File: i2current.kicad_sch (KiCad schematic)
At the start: 44 parts, among them J1 Jack-DC, J2 USB_C_Receptacle_USB2.0, J3 CONN_BATT, SW1 SW_SPDT, U1 TPS61022, U2 BQ25606RGER, U3 SPX3819M5-L-3-3, U4 FUSB302B01MPX

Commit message: save before charger replace
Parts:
- removed D2: D_Schottky, Diode_SMD:D_SMA, symbol Device:D_Schottky
- removed J1: Jack-DC, Connector_BarrelJack:BarrelJack_CUI_PJ-102AH_Horizontal, symbol Connector:Jack-DC
- added J1: Barrel_Jack_Switch, Connector_BarrelJack:BarrelJack_Wuerth_6941xx301002, symbol Connector:Barrel_Jack_Switch
- added Q1: WST03P06, Package_TO_SOT_SMD:SOT-23, symbol Critbit_lib:WST03P06
- added R4: 10k, Resistor_SMD:R_0402_1005Metric, symbol Device:R_Small
- added U4: ~, Critbit_lib:OLED_4Pin_128x64_new, symbol Critbit_lib:OLED_4Pin
- added U6: XT30(2+2)PW-M.G.B, crap:CONN-TH_4P-XT30PW-M, symbol easyeda2kicad:XT30(2+2)PW-M.G.B
- added U8: BQ25792RQMR, easyeda2kicad:QFN-29_L4.0-W4.0-P0.40-TL-BQ25792RQMR, symbol easyeda2kicad:BQ25792RQMR
- D1: value D_Schottky -> 1N5819WS; footprint Diode_SMD:D_SMA -> Diode_SMD:D_SOD-323; LCSC (none) -> C191023
- J3: footprint (none) -> Connector_JST:JST_XH_S3B-XH-A_1x03_P2.50mm_Horizontal
- L1, L2: footprint (none) -> Inductor_SMD:L_AVX_LMLP07A7
- renumbered D3 to D2, R9 to R10, R10 to R11, R11 to R12, R12 to R13, R13 to R14, R4 to R5, R5 to R6, R6 to R7, R7 to R8, R8 to R9, U4 to U5
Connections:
- net +BATT: now also U6.1
- net BAT: now also U8.22 (BAT), U8.23 (BAT)
- net GND: now also J1.2
- net VBUS: now also JP3.2 (B), Q1.3 (S), R4.2, U8.2 (VBUS), U8.3 (VBUS); no longer JP3.1 (A)
- net BQ_PWR: now reaches C1.1, D1.1 (K), U2.1 (VAC), U2.24 (VBUS)
- net BQ_PWR: now also JP1.1 (A), JP3.1 (A), Q1.2 (D); no longer JP1.2 (B), JP3.2 (B)
- net at D1.2 (A): now also JP1.2 (B), J1.1; no longer JP1.1 (A)
- new net PUSB_OFF: J1.3, Q1.1 (G), R4.1
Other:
- moved on the sheet: C1, C10, C2, C3, C4, C5, C6, C7, C8, C9, D2, J3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

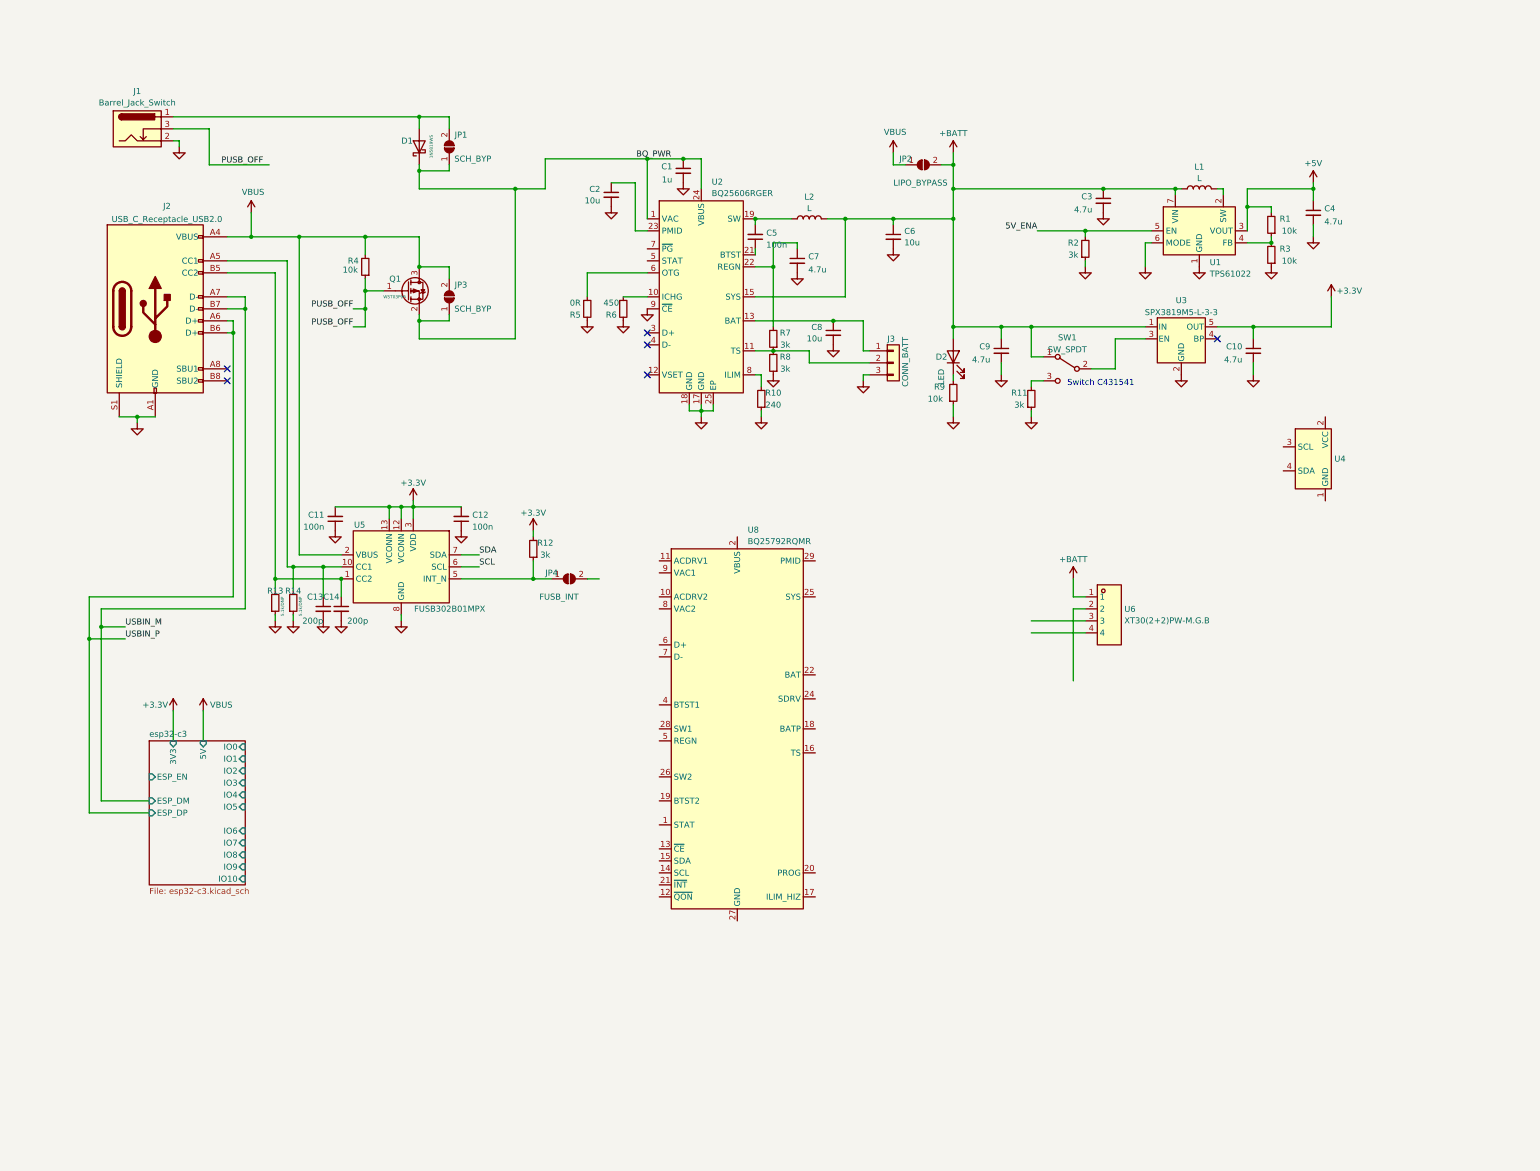
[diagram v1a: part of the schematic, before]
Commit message: connector placement
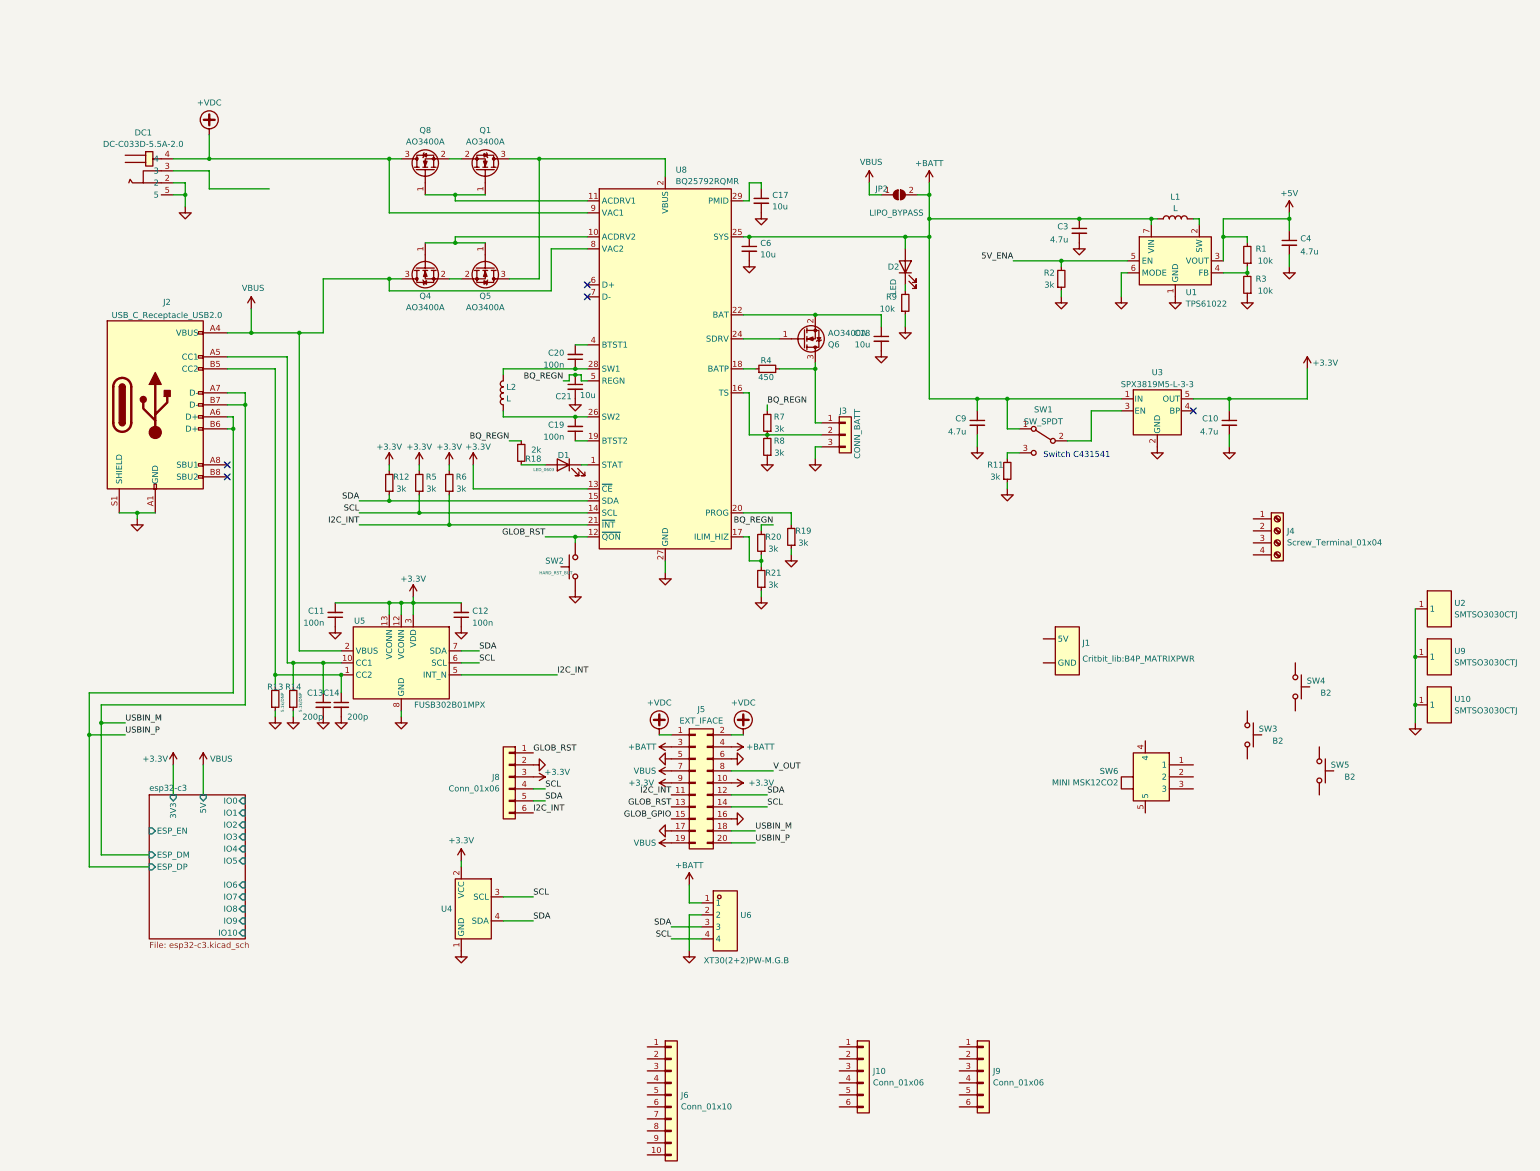
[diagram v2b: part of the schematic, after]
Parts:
- removed C1: 1u, Capacitor_SMD:C_0402_1005Metric, symbol Device:C_Small
- removed C2, C8: 10u, Capacitor_SMD:C_0402_1005Metric, symbol Device:C_Small
- removed C5: 100n, Capacitor_SMD:C_0402_1005Metric, symbol Device:C_Small
- removed C7: 4.7u, Capacitor_SMD:C_0402_1005Metric, symbol Device:C_Small
- removed D1: 1N5819WS, Diode_SMD:D_SOD-323, symbol Device:D_Schottky
- removed J1: Barrel_Jack_Switch, Connector_BarrelJack:BarrelJack_Wuerth_6941xx301002, symbol Connector:Barrel_Jack_Switch
- removed JP1, JP3: SCH_BYP, Jumper:SolderJumper-2_P1.3mm_Open_TrianglePad1.0x1.5mm, symbol Jumper:SolderJumper_2_Open
- removed JP4: FUSB_INT, Jumper:SolderJumper-2_P1.3mm_Open_TrianglePad1.0x1.5mm, symbol Jumper:SolderJumper_2_Open
- removed Q1: WST03P06, Package_TO_SOT_SMD:SOT-23, symbol Critbit_lib:WST03P06
- removed R10: 240, Resistor_SMD:R_0402_1005Metric, symbol Device:R_Small
- removed U2: BQ25606RGER, easyeda2kicad:VQFN-24_L4.0-W4.0-P0.50-TL-EP2.8, symbol easyeda2kicad:BQ25606RGER
- added C17, C18, C21: 10u, Capacitor_SMD:C_0402_1005Metric, symbol Device:C_Small
- added C19, C20: 100n, Capacitor_SMD:C_0402_1005Metric, symbol Device:C_Small
- added D1: LED_0603, LED_SMD:LED_0603_1608Metric_Pad1.05x0.95mm_HandSolder, symbol Device:LED
- added DC1: DC-C033D-5.5A-2.0, easyeda2kicad:DC-IN-TH_DC-C033D-5.5A-2.5, symbol easyeda2kicad:DC-C033D-5.5A-2.0
- added J1: ~, Critbit_lib:B4P_MATRIXPWR, symbol Critbit_lib:MATRIXPWR
- added J10, J9: Conn_01x06, Connector_JST:JST_PH_S6B-PH-K_1x06_P2.00mm_Horizontal, symbol Connector_Generic:Conn_01x06
- added J4: Screw_Terminal_01x04, TerminalBlock:TerminalBlock_bornier-4_P5.08mm, symbol Connector:Screw_Terminal_01x04
- added J5: EXT_IFACE, Critbit_lib:2x10_smdthrough, symbol Connector_Generic:Conn_02x10_Odd_Even
- added J6: Conn_01x10, Connector_Molex:Molex_PicoBlade_53261-1071_1x10-1MP_P1.25mm_Horizontal, symbol Connector_Generic:Conn_01x10
- added J8: Conn_01x06, Connector_PinHeader_2.54mm:PinHeader_1x06_P2.54mm_Vertical, symbol Connector_Generic:Conn_01x06
- added Q1, Q4, Q5, Q6, Q8: AO3400A, Package_TO_SOT_SMD:SOT-23, symbol Transistor_FET:AO3400A
- added R18: 2k, Resistor_SMD:R_0402_1005Metric, symbol Device:R_Small
- added R19, R20, R21: 3k, Resistor_SMD:R_0402_1005Metric, symbol Device:R_Small
- added SW2: HARD_RST_BUT, Button_Switch_SMD:SW_SPST_TL3342, symbol Switch:SW_Push
- added SW3, SW4, SW5: B2, Button_Switch_SMD:SW_SPST_EVQP7C, symbol Switch:SW_Push
- added SW6: MINI MSK12CO2, easyeda2kicad:SW-SMD_MSK12CO2, symbol easyeda2kicad:MINIMSK12CO2
- added U10, U2, U9: SMTSO3030CTJ, easyeda2kicad:SMD_BD5.6-D4.1, symbol easyeda2kicad:SMTSO3030CTJ
- J3: footprint Connector_JST:JST_XH_S3B-XH-A_1x03_P2.50mm_Horizontal -> Connector_JST:JST_PH_S3B-PH-K_1x03_P2.00mm_Horizontal
- R4: value 10k -> 450; LCSC C25744 -> C25890
- R5: value 0R -> 3k
- R6: value 450 -> 3k
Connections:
- net PUSB_OFF is gone; now on an unnamed net: R4.1
- net +3.3V: now also R5.2, R6.2, U4.2 (VCC), U8.13 (~{CE}), J5.10 (Pin_10), J5.9 (Pin_9), J8.3 (Pin_3)
- net +BATT: now also U8.25 (SYS), J5.3 (Pin_3), J5.4 (Pin_4); no longer L2.2
- net BAT: now also C18.1, Q6.2 (S); no longer J3.1 (Pin_1)
- net GND: now also U4.1 (GND), U6.2, U8.27 (GND), C17.2, C18.2, C21.2, DC1.2, DC1.5, J5.16 (Pin_16), J5.17 (Pin_17), J5.5 (Pin_5), J5.6 (Pin_6), J8.2 (Pin_2), R19.1, R21.1, SW2.1, U10.1, U2.1, U9.1; no longer R5.2, R6.2
- net SCL: now also R5.1, U4.3 (SCL), U6.4, U8.14 (SCL), J5.14 (Pin_14), J8.4 (Pin_4)
- net SDA: now also R12.1, U4.4 (SDA), U6.3, U8.15 (SDA), J5.12 (Pin_12), J8.5 (Pin_5)
- net USBIN_M: now also J5.18 (Pin_18)
- net USBIN_P: now also J5.20 (Pin_20)
- net VBUS: now also U8.8 (VAC2), J5.19 (Pin_19), J5.7 (Pin_7), Q1.3 (D), Q4.3 (D), Q5.3 (D); no longer R4.2
- net at L2.1: now also U8.26 (SW2), C19.2
- net I2C_INT: now reaches R6.1
- net I2C_INT: now also U5.5 (INT_N), U8.21 (~{INT}), J5.11 (Pin_11), J8.6 (Pin_6)
- net at J3.2 (Pin_2), R7.1, R8.2: now also U8.16 (TS)
- net BQ_REGN: now reaches R7.2
- net BQ_REGN: now also U8.5 (REGN), C21.1, R18.1, R20.2
- net at U8.1 (STAT): now also D1.1 (K)
- net at U8.10 (ACDRV2): now also Q4.1 (G), Q5.1 (G)
- net at U8.11 (ACDRV1): now also Q1.1 (G), Q8.1 (G)
- net GLOB_RST: now reaches U8.12 (~{QON})
- net GLOB_RST: now also J5.13 (Pin_13), J8.1 (Pin_1), SW2.2
- net at U8.17 (ILIM_HIZ): now also R20.1, R21.2
- net at U8.19 (BTST2): now also C19.1
- net at U8.20 (PROG): now also R19.2
- net at U8.24 (SDRV): now also Q6.1 (G)
- net at U8.28 (SW1): now also L2.2, C20.1
- net at U8.29 (PMID): now also C17.1
- net at U8.4 (BTST1): now also C20.2
- net +VDC: now reaches U8.9 (VAC1)
- net +VDC: now also DC1.4, J5.1 (Pin_1), J5.2 (Pin_2), Q8.3 (D)
- new net: Q4.2 (S), Q5.2 (S)
- new net: J3.1 (Pin_1), Q6.3 (D), R4.2
- new net: Q1.2 (S), Q8.2 (S)
- new net: D1.2 (A), R18.2
- new net GLOB_GPIO: J5.15 (Pin_15)
- new net V_OUT: J5.8 (Pin_8)
- no-connect marks 6 -> 5
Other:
- moved on the sheet: C10, C11, C12, C13, C14, C3, C4, C6, C9, D2, J2, J3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

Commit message: adadadadadadadadadada
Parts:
- removed J10: Conn_01x06, Connector_JST:JST_PH_S6B-PH-K_1x06_P2.00mm_Horizontal, symbol Connector_Generic:Conn_01x06
- removed J4: Screw_Terminal_01x04, TerminalBlock:TerminalBlock_bornier-4_P5.08mm, symbol Connector:Screw_Terminal_01x04
- removed L2: L, Inductor_SMD:L_AVX_LMLP07A7, symbol Device:L
- removed R11: 3k, Resistor_SMD:R_0402_1005Metric, symbol Device:R_Small
- removed R14: 5.1k/DNP, Resistor_SMD:R_0201_0603Metric, symbol Device:R_Small
- removed SW1: SW_SPDT, Button_Switch_SMD:SW_SPDT_PCM12, symbol Switch:SW_SPDT
- removed SW5: B2, Button_Switch_SMD:SW_SPST_EVQP7C, symbol Switch:SW_Push
- removed SW6: MINI MSK12CO2, easyeda2kicad:SW-SMD_MSK12CO2, symbol easyeda2kicad:MINIMSK12CO2
- removed U4: ~, Critbit_lib:OLED_4Pin_128x64_new, symbol Critbit_lib:OLED_4Pin
- added C1, C2: 100n, Capacitor_SMD:C_0402_1005Metric, symbol Device:C_Small
- added J11, J12: Screw_Terminal_01x02, TerminalBlock_MetzConnect:TerminalBlock_MetzConnect_Type086_RT03402HBLC_1x02_P3.81mm_Horizontal, symbol Connector:Screw_Terminal_01x02
- added L3: FXL0420-1R0-M, easyeda2kicad:IND-SMD_L4.4-W4.2, symbol easyeda2kicad:FXL0420-1R0-M
- added R10: 5.1k/DNP, Resistor_SMD:R_0603_1608Metric_Pad0.98x0.95mm_HandSolder, symbol Device:R_Small
- added SW6: SW_SPDT, Button_Switch_THT:SW_Slide_SPDT_Angled_CK_OS102011MA1Q, symbol Switch:SW_SPDT
- C10, C17, C18, C21, C3, C4, C6, C9: LCSC C19702 -> (none)
- C11, C12, C19, C20: LCSC C307331 -> (none)
- C13, C14: LCSC C1530 -> (none)
- JP2: LCSC DNP -> (none)
- R1, R3, R9: LCSC C25768 -> (none)
- R12, R19, R20, R21, R4, R5, R6, R7, R8: LCSC C25890 -> (none)
- R13: footprint Resistor_SMD:R_0201_0603Metric -> Resistor_SMD:R_0603_1608Metric_Pad0.98x0.95mm_HandSolder; LCSC C25117 -> (none)
- SW3, SW4: footprint Button_Switch_SMD:SW_SPST_EVQP7C -> Button_Switch_SMD:SW_SPST_TL3342
- U5: LCSC C132291 -> (none)
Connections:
- net V_OUT is gone; now on net I2C_INT: J5.8 (Pin_8)
- net +3.3V: now also J6.5 (Pin_5)
- net +BATT: now also J6.2 (Pin_2), U3.3 (EN)
- net +VDC: now also J6.1 (Pin_1)
- net GLOB_RST: now also J5.11 (Pin_11); no longer J5.13 (Pin_13)
- net GND: now also J6.3 (Pin_3), J6.8 (Pin_8), J9.1 (Pin_1), SW3.1, SW4.1, C1.2, C2.2, R10.1
- net I2C_INT: now also J6.4 (Pin_4); no longer J5.11 (Pin_11)
- net SCL: now also J6.7 (Pin_7)
- net SDA: now also J6.6 (Pin_6)
- net USBIN_M: now also J6.9 (Pin_9), J9.3 (Pin_3)
- net USBIN_P: now also J6.10 (Pin_10), J9.4 (Pin_4)
- net VBUS: now also J9.6 (Pin_6); no longer Q1.3 (D), Q5.3 (D), U8.2 (VBUS), U8.3 (VBUS)
- net esp32-c3/ESP_EN: now also SW3.2, C1.1
- net esp32-c3/IO9: now also SW4.2, C2.1
- net CC2: now reaches J2.B5 (CC2), R13.2, U5.1 (CC2), U5.14 (CC2)
- net CC2: now also C13.1, J9.5 (Pin_5); no longer C14.1
- net at C19.2, U8.26 (SW2): now also L3.2
- net at C20.1, U8.28 (SW1): now also L3.1
- net CC1: now reaches J9.2 (Pin_2)
- net CC1: now also C14.1, J2.A5 (CC1), U5.10 (CC1), U5.11 (CC1), R10.2
- net GLOB_GPIO renamed GLOB_GPIO2
- new net GLOB_GPIO1: J5.13 (Pin_13)
- new net VBUS_PIN: Q1.3 (D), Q5.3 (D), U8.2 (VBUS_PIN), U8.3 (VBUS_PIN)
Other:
- note added: "C157919"
- note added: "C393937"
- note added: "C500113"
- note removed: "Switch C431541"
- moved on the sheet: C10, C11, C12, C13, C14, C20, C21, C9, J1, J5, J6, J8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

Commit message: do backup kids
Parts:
- removed J11, J12: Screw_Terminal_01x02, TerminalBlock_MetzConnect:TerminalBlock_MetzConnect_Type086_RT03402HBLC_1x02_P3.81mm_Horizontal, symbol Connector:Screw_Terminal_01x02
- removed L1: L, Inductor_SMD:L_AVX_LMLP07A7, symbol Device:L
- removed SW2: HARD_RST_BUT, Button_Switch_SMD:SW_SPST_TL3342, symbol Switch:SW_Push
- removed U1: TPS61022, Package_DFN_QFN:Texas_RWU0007A_VQFN-7_2x2mm_P0.5mm, symbol Converter_DCDC:TPS61022
- removed U3: SPX3819M5-L-3-3, Package_TO_SOT_SMD:SOT-23-5, symbol Regulator_Linear:SPX3819M5-L-3-3
- removed U6: XT30(2+2)PW-M.G.B, crap:CONN-TH_4P-XT30PW-M, symbol easyeda2kicad:XT30(2+2)PW-M.G.B
- added C22, C25, C27, C35, C36, C38, C7, C8: 100n, Capacitor_SMD:C_0402_1005Metric, symbol Device:C_Small
- added C23, C24, C28: 22uF, Capacitor_SMD:C_0603_1608Metric, symbol Device:C_Small
- added C26, C31, C32, C33, C34, C37, C39, C40, C41, C42, C5: 10u, Capacitor_SMD:C_0603_1608Metric, symbol Device:C_Small
- added C29, C30: 2u2, Capacitor_SMD:C_0603_1608Metric, symbol Device:C_Small
- added D3: 1N5819WS, Diode_SMD:D_SOD-323, symbol Device:D_Schottky
- added J10, J11: QWIIC, Connector_JST:JST_SH_SM04B-SRSS-TB_1x04-1MP_P1.00mm_Horizontal, symbol Connector_Generic:Conn_01x04
- added J4: BIG_OUT, TerminalBlock_MetzConnect:TerminalBlock_MetzConnect_Type086_RT03406HBLC_1x06_P3.81mm_Horizontal, symbol Connector:Screw_Terminal_01x06
- added JP1: HARDRST, Jumper:SolderJumper-2_P1.3mm_Open_TrianglePad1.0x1.5mm, symbol Jumper:SolderJumper_2_Open
- added L1: IHLP3232DZER3R3M11, easyeda2kicad:IND-SMD_L8.7-W8.2_IHLP-3232CZ, symbol easyeda2kicad:IHLP3232DZER3R3M11
- added L4: FXL0630-6R8-M, easyeda2kicad:IND-SMD_L7.0-W6.6, symbol easyeda2kicad:FXL0630-6R8-M
- added R11, R14, R16, R17: 3k, Resistor_SMD:R_0402_1005Metric, symbol Device:R_Small
- added R22: 450, Resistor_SMD:R_0402_1005Metric, symbol Device:R_Small
- added R23, R24: 2, Resistor_SMD:R_0402_1005Metric, symbol Device:R_Small
- added U11: TPS56637RPAR, easyeda2kicad:VQFN-HR-10_L3.0-W3.0_RPA, symbol easyeda2kicad:TPS56637RPAR
- added U3: SMTSO3030CTJ, easyeda2kicad:SMD_BD5.6-D4.1, symbol easyeda2kicad:SMTSO3030CTJ
- added U4: TPS5430DDA, Package_SO:SOIC-8_3.9x4.9mm_P1.27mm, symbol Critbit_lib:TPS54331
- C10, C9: value 4.7u -> 100n
- C17, C18, C6: footprint Capacitor_SMD:C_0402_1005Metric -> Capacitor_SMD:C_0603_1608Metric
- C21: value 10u -> 4.7u/10V
- C3: value 4.7u -> 22uF; footprint Capacitor_SMD:C_0402_1005Metric -> Capacitor_SMD:C_0603_1608Metric
- C4: value 4.7u -> 10u; footprint Capacitor_SMD:C_0402_1005Metric -> Capacitor_SMD:C_0603_1608Metric
- R1: value 10k -> 73.2k
- R19: footprint Resistor_SMD:R_0402_1005Metric -> Resistor_SMD:R_0603_1608Metric_Pad0.98x0.95mm_HandSolder
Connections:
- net +3.3V: now also C3.1, C23.1, C24.1, C28.1, J10.2 (Pin_2), J11.2 (Pin_2), L4.1, R11.2; no longer C10.1, U8.13 (~{CE})
- net +5V: now also J1.5V, C41.1, C42.1, L1.2
- net +BATT: now also C26.1, C27.2, C31.1, C32.1, C36.2, C37.1, C5.1, C7.2, J4.1 (Pin_1), R22.2, U11.8 (VIN), U4.2 (VIN); no longer C3.1, C9.1, D2.2 (A)
- net +VDC: now also J4.3 (Pin_3), R23.2
- net 5V_ENA: now also R2.1, U11.1 (EN); no longer R2.2
- net BQ_REGN: now also U8.13 (~{CE})
- net GLOB_RST: no longer J5.11 (Pin_11), U8.12 (~{QON})
- net GND: now also C10.1, C9.1, J1.GND, SW6.3 (C), C23.2, C24.2, C26.2, C27.1, C28.2, C29.2, C30.2, C31.2, C32.2, C33.2, C34.2, C35.1, C36.1, C37.2, C38.1, C39.2, C40.2, C41.2, C42.2, C5.2, C7.1, D3.2 (A), J10.1 (Pin_1), J11.1 (Pin_1), J4.4 (Pin_4), JP1.2 (B), R14.1, R16.1, U11.10 (MODE), U11.3 (AGND), U11.9 (PGND), U4.7 (GND); no longer C10.2, C9.2, R2.1
- net SCL: now also J10.4 (Pin_4), J11.4 (Pin_4)
- net SDA: now also J10.3 (Pin_3), J11.3 (Pin_3)
- net USBIN_M: now also J6.10 (Pin_10); no longer J6.9 (Pin_9)
- net USBIN_P: now also J6.9 (Pin_9); no longer J6.10 (Pin_10)
- net VBUS: now also R24.2
- net VBUS_PIN: now also C38.2, C39.1, C40.1
- net at SW6.1 (A): now also R22.1
- net GLOB_~{OFF}: now reaches SW6.2 (B)
- net GLOB_~{OFF}: now also D2.2 (A), J5.11 (Pin_11), R2.2, J4.2 (Pin_2), R17.2
- net at R1.1, R3.2: now also U11.2 (FB)
- net BAT_IN: now reaches J3.1 (Pin_1), Q6.3 (D), R4.2
- net BAT_IN: now also J4.6 (Pin_6)
- net LIPO_NTC: now reaches J3.2 (Pin_2), R7.1, R8.2, U8.16 (TS)
- net LIPO_NTC: now also J4.5 (Pin_5)
- net at C17.1, U8.29 (PMID): now also C33.1, C34.1, C35.2
- new net: C30.1, R24.1
- new net: C8.1, D3.1 (K), L4.2, U4.8 (PH)
- new net: C29.1, R23.1
- new net: C8.2, U4.1 (BOOT)
- new net: R17.1, U4.3 (EN)
- new net: C9.2, U4.4 (SS)
- new net: R11.1, R14.2, U4.5 (VSENSE)
- new net: C10.2, C22.2, U4.6 (COMP)
- new net: JP1.1 (A), U8.12 (~{QON})
- new net: C22.1, R16.2
- new net: C25.2, L1.1, U11.6 (SW)
- new net: C25.1, U11.7 (BOOT)
- no-connect marks 5 -> 4
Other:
- note added: "C2908435"
- note added: "C69810"
- note added: "Rprog 1.5MHz settings: 1S - 3k 2S - 6.04k 3S - 10.5k 4S - 17.4k"
- moved on the sheet: C6, D2, J1, J3, R1, R2, R3, R9, SW6
